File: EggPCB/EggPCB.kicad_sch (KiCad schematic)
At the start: 17 parts, among them J1 Photocell_1_V+, J2 Photocell_2_V+, J3 Photocell_1_V-, J4 Photocell_2_V-, J5 Conn_01x02_Pin, J6 Conn_01x02_Pin, J7 Photocell_1_V-, J8 GND VIA

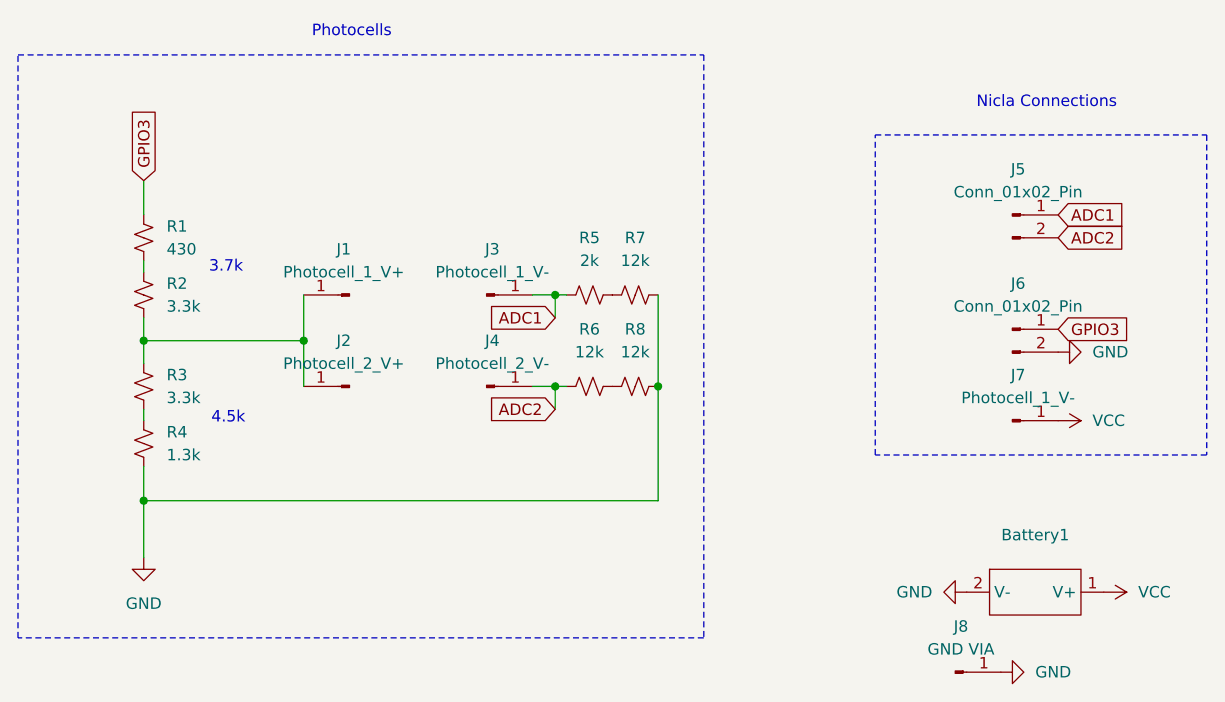
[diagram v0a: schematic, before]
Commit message: Nicla to Raspi connection should be working
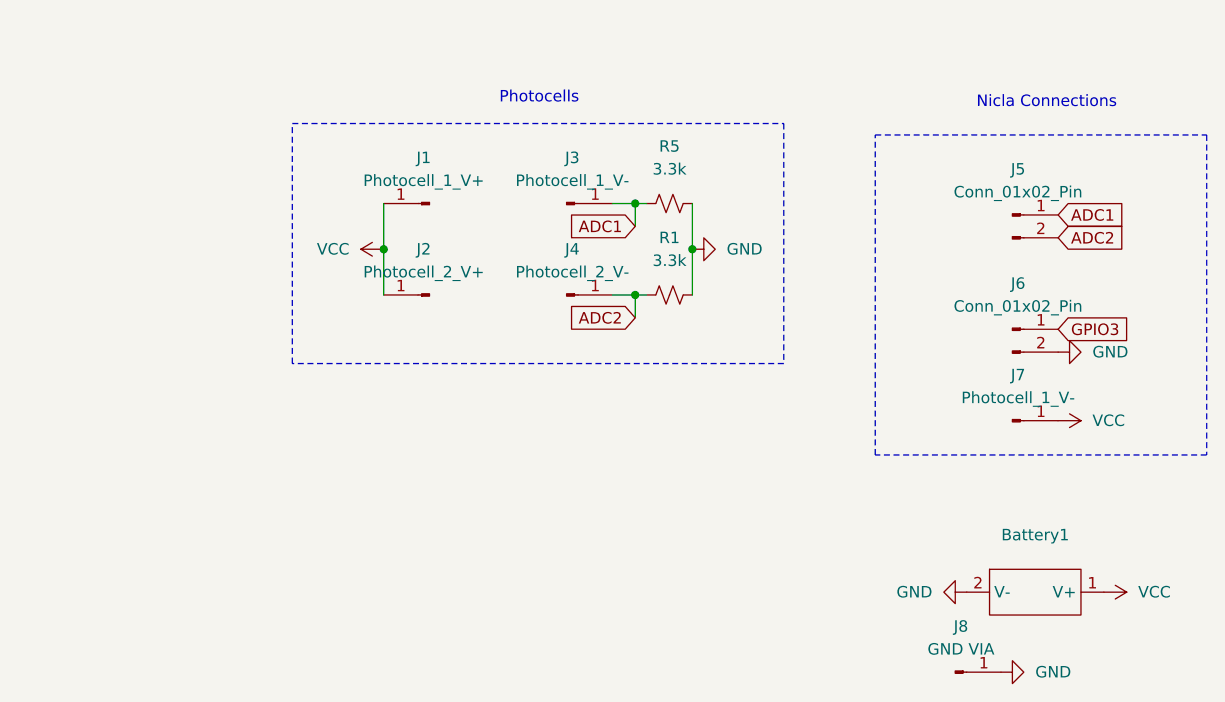
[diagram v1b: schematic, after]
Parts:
- removed R2, R3: 3.3k, Resistor_SMD:R_0603_1608Metric_Pad0.98x0.95mm_HandSolder, symbol Device:R_Small_US
- removed R4: 1.3k, Resistor_SMD:R_0603_1608Metric_Pad0.98x0.95mm_HandSolder, symbol Device:R_Small_US
- removed R6, R7, R8: 12k, Resistor_SMD:R_0603_1608Metric_Pad0.98x0.95mm_HandSolder, symbol Device:R_Small_US
- R1: value 430 -> 3.3k
- R5: value 2k -> 3.3k
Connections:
- net ADC2: now also R1.1
- net GND: now also R1.2, R5.2
- net GPIO3: no longer R1.1
- net VCC: now also J1.1 (Pin_1), J2.1 (Pin_1)
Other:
- note removed: "3.7k"
- note removed: "4.5k"
- moved on the sheet: J1, J2, J3, J4, R5

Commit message: Work over past few days
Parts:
- removed J8: GND VIA, Connector_PinHeader_2.54mm:PinHeader_1x01_P2.54mm_Vertical, symbol Connector:Conn_01x01_Pin
- R1, R5: footprint Resistor_SMD:R_0603_1608Metric_Pad0.98x0.95mm_HandSolder -> Resistor_THT:R_Axial_DIN0207_L6.3mm_D2.5mm_P7.62mm_Horizontal
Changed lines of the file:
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@@
 			)
 		)
-		(property "Footprint" "Resistor_SMD:R_0603_1608Metric_Pad0.98x0.95mm_HandSolder"
+		(property "Footprint" "Resistor_THT:R_Axial_DIN0207_L6.3mm_D2.5mm_P7.62mm_Horizontal"
 			(at 130.81 38.1 0)
 			(effects
@@
 	)
 	(symbol
-		(lib_id "power:GND")
-		(at 167.64 90.17 90)
-		(unit 1)
-		(exclude_from_sim no)
-		(in_bom yes)
-		(on_board yes)
-		(dnp no)
-		(fields_autoplaced yes)
-		(property "Reference" "#PWR01"
-			(at 173.99 90.17 0)
-			(effects
-				(font
-					(size 1.27 1.27)
-				)
-				(hide yes)
-			)
-		)
-		(property "Value" "GND"
-			(at 171.45 90.1699 90)
-			(effects
-				(font
-					(size 1.27 1.27)
-				)
-				(justify right)
-			)
-		)
-		(property "Footprint" ""
-			(at 167.64 90.17 0)
-			(effects
-				(font
-					(size 1.27 1.27)
-				)
-				(hide yes)
-			)
-		)
-		(property "Datasheet" ""
-			(at 167.64 90.17 0)
-			(effects
-				(font
-					(size 1.27 1.27)
-				)
-				(hide yes)
-			)
-		)
-		(property "Description" "Power symbol creates a global label with name \"GND\" , ground"
-			(at 167.64 90.17 0)
-			(effects
-				(font
-					(size 1.27 1.27)
-				)
-				(hide yes)
-			)
-		)
-		(pin "1"
-		)
-		(instances
-			(project "EggPCB"
-				(path "/598ec87c-13c0-448b-bf4d-0435f996b9ec"
-					(reference "#PWR01")
-					(unit 1)
-				)
-			)
-		)
-	)
-	(symbol
-		(lib_id "Connector:Conn_01x01_Pin")
-		(at 162.56 90.17 0)
-		(unit 1)
-		(exclude_from_sim no)
-		(in_bom yes)
-		(on_board yes)
-		(dnp no)
-		(fields_autoplaced yes)
-		(property "Reference" "J8"
-			(at 163.195 85.09 0)
-			(effects
-				(font
-					(size 1.27 1.27)
-				)
-			)
-		)
-		(property "Value" "GND VIA"
-			(at 163.195 87.63 0)
-			(effects
-				(font
-					(size 1.27 1.27)
-				)
-			)
-		)
-		(property "Footprint" "Connector_PinHeader_2.54mm:PinHeader_1x01_P2.54mm_Vertical"
-			(at 162.56 90.17 0)
-			(effects
-				(font
-					(size 1.27 1.27)
-				)
-				(hide yes)
-			)
-		)
-		(property "Datasheet" "~"
-			(at 162.56 90.17 0)
-			(effects
-				(font
-					(size 1.27 1.27)
-				)
-				(hide yes)
-			)
-		)
-		(property "Description" "Generic connector, single row, 01x01, script generated"
-			(at 162.56 90.17 0)
-			(effects
-				(font
-					(size 1.27 1.27)
-				)
-				(hide yes)
-			)
-		)
-		(pin "1"
-		)
-		(instances
-			(project "EggPCB"
-				(path "/598ec87c-13c0-448b-bf4d-0435f996b9ec"
-					(reference "J8")
-					(unit 1)
-				)
-			)
-		)
-	)
-	(symbol
 		(lib_id "Connector:Conn_01x01_Pin")
 		(at 168.91 62.23 0)
@@
 			)
 		)
-		(property "Footprint" "Resistor_SMD:R_0603_1608Metric_Pad0.98x0.95mm_HandSolder"
+		(property "Footprint" "Resistor_THT:R_Axial_DIN0207_L6.3mm_D2.5mm_P7.62mm_Horizontal"
 			(at 130.81 48.26 0)
 			(effects

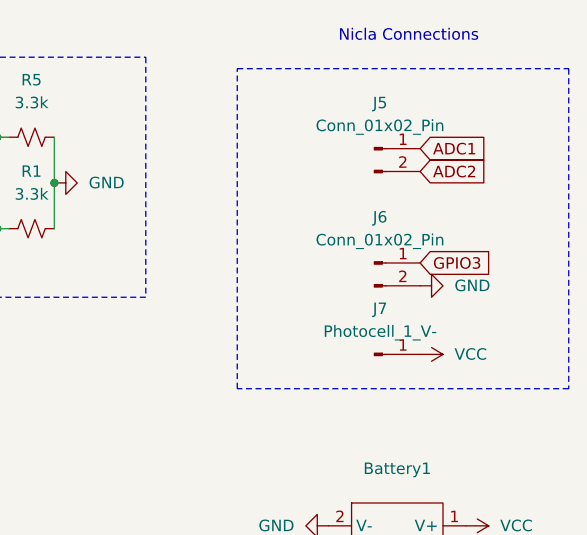
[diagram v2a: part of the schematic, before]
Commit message: Updates to pcb to remove GPIO3 pin
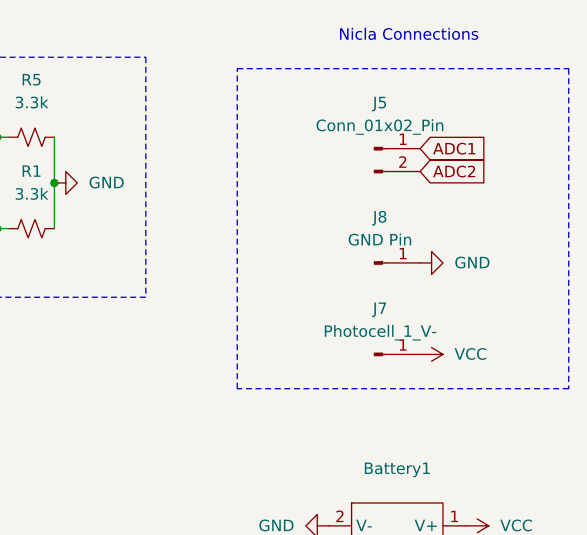
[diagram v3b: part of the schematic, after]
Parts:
- removed J6: Conn_01x02_Pin, Connector_PinHeader_2.54mm:PinHeader_1x02_P2.54mm_Vertical, symbol Connector:Conn_01x02_Pin
- added J8: GND Pin, Connector_PinHeader_2.54mm:PinHeader_1x01_P2.54mm_Vertical, symbol Connector:Conn_01x01_Pin
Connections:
- net GND: now also J8.1 (Pin_1)
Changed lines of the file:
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@@
 		)
 	)
-	(global_label "GPIO3"
+	(global_label "ADC2"
 		(shape input)
-		(at 173.99 52.07 0)
+		(at 173.99 41.91 0)
 		(fields_autoplaced yes)
 		(effects
@@
 		)
 		(property "Intersheetrefs" "${INTERSHEET_REFS}"
-			(at 182.66 52.07 0)
+			(at 181.8133 41.91 0)
 			(effects
 				(font
@@
 		)
 	)
-	(global_label "ADC2"
+	(global_label "ADC1"
 		(shape input)
-		(at 173.99 41.91 0)
+		(at 173.99 39.37 0)
 		(fields_autoplaced yes)
 		(effects
@@
 		)
 		(property "Intersheetrefs" "${INTERSHEET_REFS}"
-			(at 181.8133 41.91 0)
-			(effects
-				(font
-					(size 1.27 1.27)
-				)
-				(justify left)
-				(hide yes)
-			)
-		)
-	)
-	(global_label "ADC1"
-		(shape input)
-		(at 173.99 39.37 0)
-		(fields_autoplaced yes)
-		(effects
-			(font
-				(size 1.27 1.27)
-			)
-			(justify left)
-		)
-		(property "Intersheetrefs" "${INTERSHEET_REFS}"
 			(at 181.8133 39.37 0)
 			(effects
@@
 	)
 	(symbol
-		(lib_id "power:GND")
-		(at 173.99 54.61 90)
-		(unit 1)
-		(exclude_from_sim no)
-		(in_bom yes)
-		(on_board yes)
-		(dnp no)
-		(fields_autoplaced yes)
-		(property "Reference" "#PWR0105"
-			(at 180.34 54.61 0)
-			(effects
-				(font
-					(size 1.27 1.27)
-				)
-				(hide yes)
-			)
-		)
-		(property "Value" "GND"
-			(at 177.8 54.6099 90)
-			(effects
-				(font
-					(size 1.27 1.27)
-				)
-				(justify right)
-			)
-		)
-		(property "Footprint" ""
-			(at 173.99 54.61 0)
-			(effects
-				(font
-					(size 1.27 1.27)
-				)
-				(hide yes)
-			)
-		)
-		(property "Datasheet" ""
-			(at 173.99 54.61 0)
-			(effects
-				(font
-					(size 1.27 1.27)
-				)
-				(hide yes)
-			)
-		)
-		(property "Description" "Power symbol creates a global label with name \"GND\" , ground"
-			(at 173.99 54.61 0)
-			(effects
-				(font
-					(size 1.27 1.27)
-				)
-				(hide yes)
-			)
-		)
-		(pin "1"
-		)
-		(instances
-			(project "EggPCB"
-				(path "/598ec87c-13c0-448b-bf4d-0435f996b9ec"
-					(reference "#PWR0105")
-					(unit 1)
-				)
-			)
-		)
-	)
-	(symbol
 		(lib_id "Connector:Conn_01x01_Pin")
 		(at 168.91 62.23 0)
@@
 	)
 	(symbol
+		(lib_id "power:GND")
+		(at 173.99 52.07 90)
+		(unit 1)
+		(exclude_from_sim no)
+		(in_bom yes)
+		(on_board yes)
+		(dnp no)
+		(fields_autoplaced yes)
+		(property "Reference" "#PWR01"
+			(at 180.34 52.07 0)
+			(effects
+				(font
+					(size 1.27 1.27)
+				)
+				(hide yes)
+			)
+		)
+		(property "Value" "GND"
+			(at 177.8 52.0699 90)
+			(effects
+				(font
+					(size 1.27 1.27)
+				)
+				(justify right)
+			)
+		)
+		(property "Footprint" ""
+			(at 173.99 52.07 0)
+			(effects
+				(font
+					(size 1.27 1.27)
+				)
+				(hide yes)
+			)
+		)
+		(property "Datasheet" ""
+			(at 173.99 52.07 0)
+			(effects
+				(font
+					(size 1.27 1.27)
+				)
+				(hide yes)
+			)
+		)
+		(property "Description" "Power symbol creates a global label with name \"GND\" , ground"
+			(at 173.99 52.07 0)
+			(effects
+				(font
+					(size 1.27 1.27)
+				)
+				(hide yes)
+			)
+		)
+		(pin "1"
+		)
+		(instances
+			(project "EggPCB"
+				(path "/598ec87c-13c0-448b-bf4d-0435f996b9ec"
+					(reference "#PWR01")
+					(unit 1)
+				)
+			)
+		)
+	)
+	(symbol
 		(lib_id "Connector:Conn_01x01_Pin")
 		(at 119.38 48.26 0)
@@
 	)
 	(symbol
+		(lib_id "Connector:Conn_01x01_Pin")
+		(at 168.91 52.07 0)
+		(unit 1)
+		(exclude_from_sim no)
+		(in_bom yes)
+		(on_board yes)
+		(dnp no)
+		(fields_autoplaced yes)
+		(property "Reference" "J8"
+			(at 169.545 46.99 0)
+			(effects
+				(font
+					(size 1.27 1.27)
+				)
+			)
+		)
+		(property "Value" "GND Pin"
+			(at 169.545 49.53 0)
+			(effects
+				(font
+					(size 1.27 1.27)
+				)
+			)
+		)
+		(property "Footprint" "Connector_PinHeader_2.54mm:PinHeader_1x01_P2.54mm_Vertical"
+			(at 168.91 52.07 0)
+			(effects
+				(font
+					(size 1.27 1.27)
+				)
+				(hide yes)
+			)
+		)
+		(property "Datasheet" "~"
+			(at 168.91 52.07 0)
+			(effects
+				(font
+					(size 1.27 1.27)
+				)
+				(hide yes)
+			)
+		)
+		(property "Description" "Generic connector, single row, 01x01, script generated"
+			(at 168.91 52.07 0)
+			(effects
+				(font
+					(size 1.27 1.27)
+				)
+				(hide yes)
+			)
+		)
+		(pin "1"
+		)
+		(instances
+			(project "EggPCB"
+				(path "/598ec87c-13c0-448b-bf4d-0435f996b9ec"
+					(reference "J8")
+					(unit 1)
+				)
+			)
+		)
+	)
+	(symbol
 		(lib_id "power:GND")
 		(at 133.35 43.18 90)
@@
 					(unit 1)
 				)
-			)
-		)
-	)
-	(symbol
-		(lib_id "Connector:Conn_01x02_Pin")
-		(at 168.91 52.07 0)
-		(unit 1)
-		(exclude_from_sim no)
-		(in_bom yes)
-		(on_board yes)
-		(dnp no)
-		(fields_autoplaced yes)
-		(property "Reference" "J6"
-			(at 169.545 46.99 0)
-			(effects
-				(font
-					(size 1.27 1.27)
-				)
-			)
-		)
-		(property "Value" "Conn_01x02_Pin"
-			(at 169.545 49.53 0)
-			(effects
-				(font
-					(size 1.27 1.27)
-				)
-			)
-		)
-		(property "Footprint" "Connector_PinHeader_2.54mm:PinHeader_1x02_P2.54mm_Vertical"
-			(at 168.91 52.07 0)
-			(effects
-				(font
-					(size 1.27 1.27)
-				)
-				(hide yes)
-			)
-		)
-		(property "Datasheet" "~"
-			(at 168.91 52.07 0)
-			(effects
-				(font
-					(size 1.27 1.27)
-				)
-				(hide yes)
-			)
-		)
-		(property "Description" "Generic connector, single row, 01x02, script generated"
-			(at 168.91 52.07 0)
-			(effects
-				(font
-					(size 1.27 1.27)
-				)
-				(hide yes)
-			)
-		)
-		(pin "1"
-		)
-		(pin "2"
-		)
-		(instances
-			(project "EggPCB"
-				(path "/598ec87c-13c0-448b-bf4d-0435f996b9ec"
-					(reference "J6")
-					(unit 1)
-				)
